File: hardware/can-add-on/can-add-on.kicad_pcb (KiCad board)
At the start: 2 copper layers, 48 x 40 mm, 32 parts

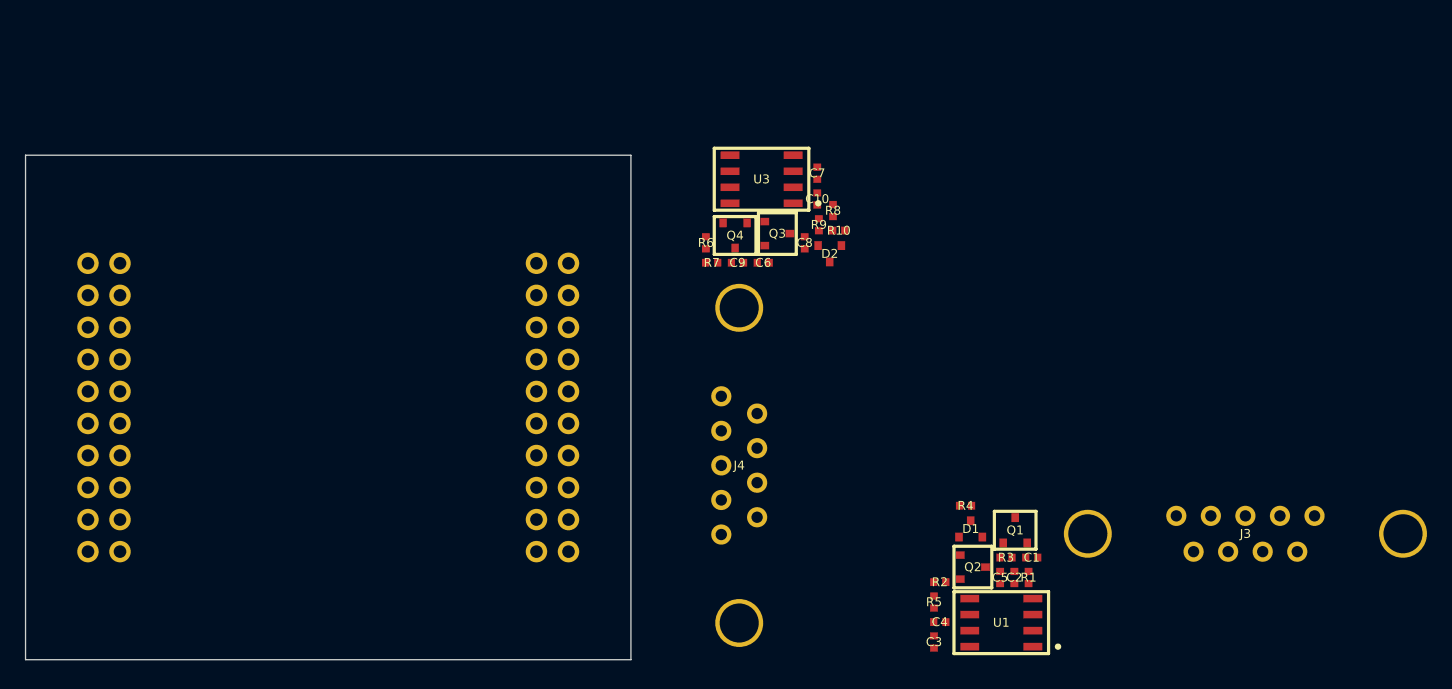
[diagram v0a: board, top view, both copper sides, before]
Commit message: Factor out glasgow
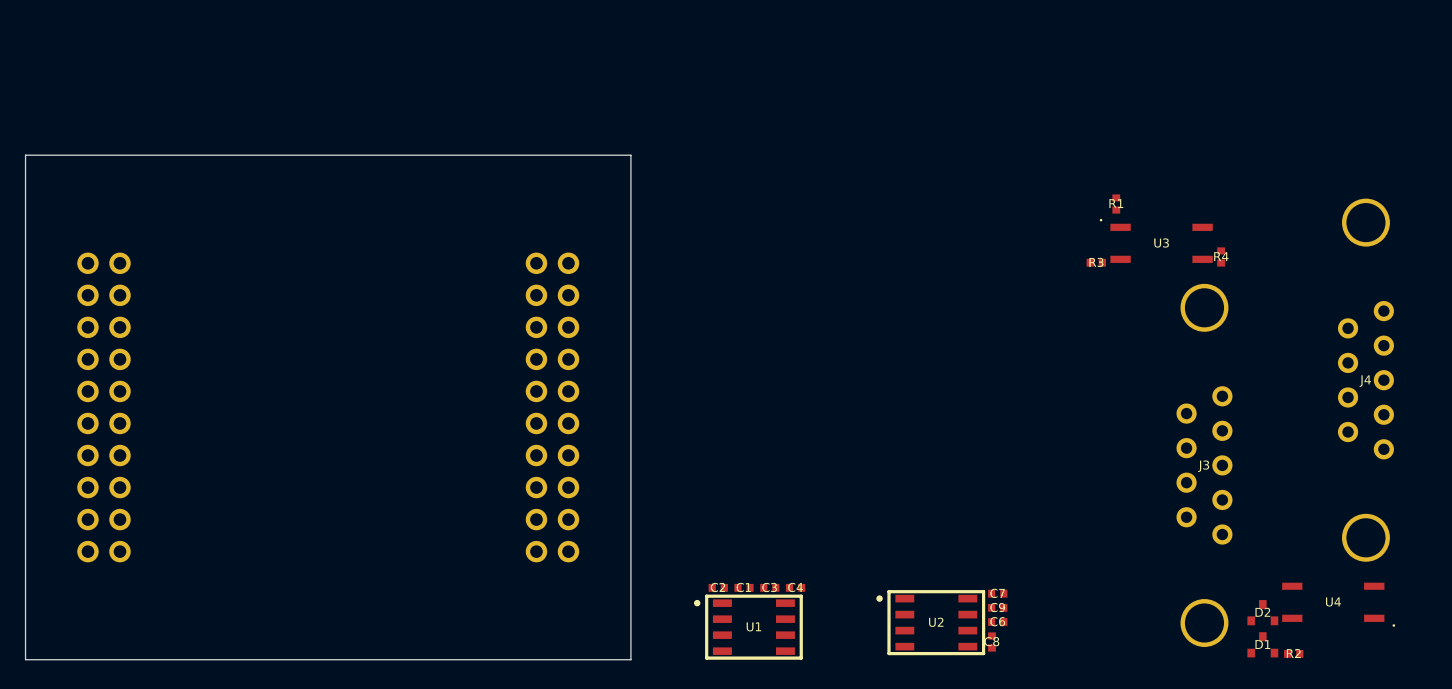
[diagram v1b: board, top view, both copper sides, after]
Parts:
- removed C10, C5, R10, R5, R6, R7, R8, R9: , can-add-on:ipc-two-pin-package$22
- removed Q1, Q2, Q3, Q4: , can-add-on:SOT95P280X100-3N
- added U2: , can-add-on:soic127p-package$19, F.Cu at (196.7, 122.1)
- added U4: , can-add-on:tlp-175, F.Cu at (228.2, 120.4)
- C1, C2, C3, C4, C6, C7, C8, C9, R1, R2, R3, R4: footprint can-add-on:ipc-two-pin-package$22 -> can-add-on:ipc-two-pin-package$24
- J1, J2: footprint can-add-on:pin-header-pkg$13 -> can-add-on:pin-header-pkg$15
- J3, J4: footprint can-add-on:amphenol-delta-d-pkg$30 -> can-add-on:amphenol-delta-d-pkg$32
- U1: footprint can-add-on:soic127p-package$17 -> can-add-on:soic127p-package$19
- U3: footprint can-add-on:soic127p-package$17 -> can-add-on:tlp-175
- moved J4 50.2 mm to (230.8, 102.8), turned to 0 degrees
- moved D2 44.6 mm to (222.6, 121.3), turned to 0 degrees
- moved C7 36.3 mm to (201.6, 119.8), turned to 0 degrees
- moved C8 35.0 mm to (201.1, 123.6), turned to 90 degrees
- moved C9 34.3 mm to (201.6, 120.9), turned to 180 degrees
- moved C6 34.0 mm to (201.6, 122.0)
- moved U3 32.1 mm to (214.6, 92.0), turned to 0 degrees
- moved R1 30.4 mm to (211.0, 88.9)
- moved R2 28.6 mm to (225.1, 124.5), turned to 0 degrees
- moved R4 28.3 mm to (219.3, 93.1), turned to 90 degrees
- moved D1 24.9 mm to (222.6, 123.8)
- moved R3 24.4 mm to (209.4, 93.5)
- moved C2 23.5 mm to (179.4, 119.3), turned to 0 degrees
- moved C1 22.9 mm to (181.5, 119.3), turned to 180 degrees
- moved U1 19.6 mm to (182.3, 122.4), turned to 0 degrees
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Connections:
- net net_can-a_vcc renamed net_xr-a_vcc
- C6 pad 1: net_can-b_vcc -> net_xr-b_vio
- C7 pad 1: net_can-b_vcc -> net_xr-b_vio
- C8 pad 1: net_can-b_vcc -> net_xr-b_vio
- C9 pad 1: net_can-b_vcc -> net_xr-b_vio
- D1 pad 1: net_can-a_j_p3 -> net_xr-a_can_canh
- D1 pad 2: net_can-a_xr_xcvr_CANL -> net_ssr$38_drain1
- D2 pad 1: net_can-b_xr_xcvr_CANH -> net_j-b_p3
- D2 pad 2: net_can-b_rid$39_p1 -> net_j-b_p5
- J1 pad 1: net_can-b_vcc -> net_xr-b_vio
- J3 pad 3: net_can-a_j_p3 -> net_xr-a_can_canh
- J3 pad 5: net_can-a_xr_xcvr_CANL -> net_ssr$38_drain1
- J4 pad 3: net_can-b_xr_xcvr_CANH -> net_j-b_p3
- J4 pad 5: net_can-b_rid$39_p1 -> net_j-b_p5
- R1 pad 1: net_can-a_j_p3 -> glasgow_PA4
- R1 pad 2: net_can-a_rid$36_p2 -> net_ssr$38_a
- R2 pad 1: net_can-a_xr_xcvr_CANL -> net_j-b_p3
- R2 pad 2: net_can-a_q$33_1_s -> net_ssr$46_drain2
- R3 pad 1: glasgow_PA3 -> net_xr-a_can_canh
- R3 pad 2: net_can-a_rid$42_p1 -> net_ssr$38_drain2
- R4 pad 1: net_can-a_rid$42_p1 -> glasgow_PB4
- R4 pad 2: gnd -> net_ssr$46_a
- U1 pad 6: net_can-a_xr_xcvr_CANL -> net_ssr$38_drain1
- U1 pad 7: net_can-a_j_p3 -> net_xr-a_can_canh
- U1 pad 8: glasgow_PA4 -> glasgow_PA3
- U3 pad 1: glasgow_PB1 -> net_ssr$38_a
- U3 pad 3: net_can-b_vcc -> gnd
- U3 pad 4: glasgow_PB2 -> net_ssr$38_drain2
- U3 pad 6: net_can-b_rid$39_p1 -> net_ssr$38_drain1

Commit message: REfactor glasgow model
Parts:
- removed D2: , can-add-on:SC-70-3
- added ?: , can-add-on:two-pin-polarized-package$58, F.Cu at (202.7, 79.7)
- added ?: , can-add-on:two-pin-polarized-package$58, F.Cu at (201.8, 81.7)
- added C10: , can-add-on:ipc-two-pin-package$30, F.Cu at (205.7, 81.7)
- added C11: , can-add-on:ipc-two-pin-package$30, F.Cu at (192.5, 123.6)
- added C12: , can-add-on:ipc-two-pin-package$30, F.Cu at (199.5, 80.1)
- added C5: , can-add-on:ipc-two-pin-package$30, F.Cu at (193.7, 100.9)
- added D4: , can-add-on:SC-70-3, F.Cu at (194.5, 103.2)
- added T1: , can-add-on:xfmr-760390012, F.Cu at (214.3, 115.9)
- added U5: , can-add-on:soic127p-package$65, F.Cu at (197.1, 118.7)
- added U6: , can-add-on:tlp-175, F.Cu at (194.1, 110.7)
- C1, C2, C3, C4, C6, C7, C8, C9, R1, R2, R3, R4: footprint can-add-on:ipc-two-pin-package$24 -> can-add-on:ipc-two-pin-package$30
- J1, J2: footprint can-add-on:pin-header-pkg$15 -> can-add-on:pin-header-pkg$19
- J3, J4: footprint can-add-on:amphenol-delta-d-pkg$32 -> can-add-on:amphenol-delta-d-pkg$38
- U1: footprint can-add-on:soic127p-package$19 -> can-add-on:soic127p-package$25
- U2: footprint can-add-on:soic127p-package$19 -> can-add-on:tlp-175
- U3: footprint can-add-on:tlp-175 -> can-add-on:soic127p-package$25
- U4: footprint can-add-on:tlp-175 -> can-add-on:SOT95P280X145-5N
- moved D1 49.5 mm to (197.2, 81.3), turned to 90 degrees
- moved R2 46.0 mm to (207.3, 82.2)
- moved U2 45.0 mm to (210.4, 79.2)
- moved C9 42.3 mm to (196.5, 78.9), turned to 270 degrees
- moved C8 41.9 mm to (199.1, 81.7)
- moved U3 31.3 mm to (206.0, 122.1)
- moved R4 28.5 mm to (193.7, 105.5)
- moved J4 25.4 mm to (205.8, 98.2)
- moved R3 24.1 mm to (197.2, 114.3)
- moved U4 24.1 mm to (204.3, 118.1), turned to 90 degrees
- moved C6 18.8 mm to (192.5, 105.5), turned to 270 degrees
- moved C7 15.8 mm to (194.8, 105.5), turned to 90 degrees
- moved J3 14.0 mm to (212.2, 96.8), turned to 180 degrees
- moved R1 9.61 mm to (204.6, 81.7)
- moved C1 6.65 mm to (185.6, 124.5), turned to 0 degrees
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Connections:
- net glasgow_PA1 renamed CANA-TX
- net glasgow_PA2 renamed CANA-RX
- net glasgow_PA3 renamed CANA-S
- net net_xr-a_vcc renamed VIO-A
- C6 pad 1: net_xr-b_vio -> VIO-B
- C7 pad 1: net_xr-b_vio -> VIO-B
- C8 pad 1: net_xr-b_vio -> VIO-B
- C9 pad 1: net_xr-b_vio -> net_iso$61_en2
- C9 pad 2: gnd -> net_iso$61_iso_GND2
- D1 pad 1: net_xr-a_can_canh -> CANA-H
- D1 pad 2: net_ssr$38_drain1 -> CANA-L
- J1 pad 1: net_xr-b_vio -> VIO-B
- J3 pad 3: net_xr-a_can_canh -> CANA-H
- J3 pad 5: net_ssr$38_drain1 -> CANA-L
- J4 pad 3: net_j-b_p3 -> net_rid$71_p1
- R1 pad 2: net_ssr$38_a -> net_ssr$44_a
- R2 pad 1: net_j-b_p3 -> CANA-H
- R2 pad 2: net_ssr$46_drain2 -> net_rid$49_p2
- R3 pad 1: net_xr-a_can_canh -> glasgow_PB4
- R3 pad 2: net_ssr$38_drain2 -> net_ssr$69_a
- R4 pad 1: glasgow_PB4 -> net_rid$71_p1
- R4 pad 2: net_ssr$46_a -> net_rid$71_p2
- U1 pad 6: net_ssr$38_drain1 -> CANA-L
- U1 pad 7: net_xr-a_can_canh -> CANA-H
- U2 pad 1: glasgow_PB1 -> net_ssr$44_a
- U2 pad 3: net_xr-b_vio -> gnd
- U2 pad 4: glasgow_PB2 -> net_rid$49_p2
- U2 pad 6: net_j-b_p5 -> CANA-L
- U3 pad 1: net_ssr$38_a -> net_xr-b_uart_tx
- U3 pad 3: gnd -> VIO-B
- U3 pad 4: net_ssr$38_drain2 -> net_xr-b_uart_rx
- U3 pad 6: net_ssr$38_drain1 -> net_j-b_p5
- U4 pad 1: net_ssr$46_a -> net_iso$51_xfrmr_p5
- U4 pad 3: gnd -> net_iso$51_xfrmr_p1
- U4 pad 4: net_ssr$46_drain2 -> gnd

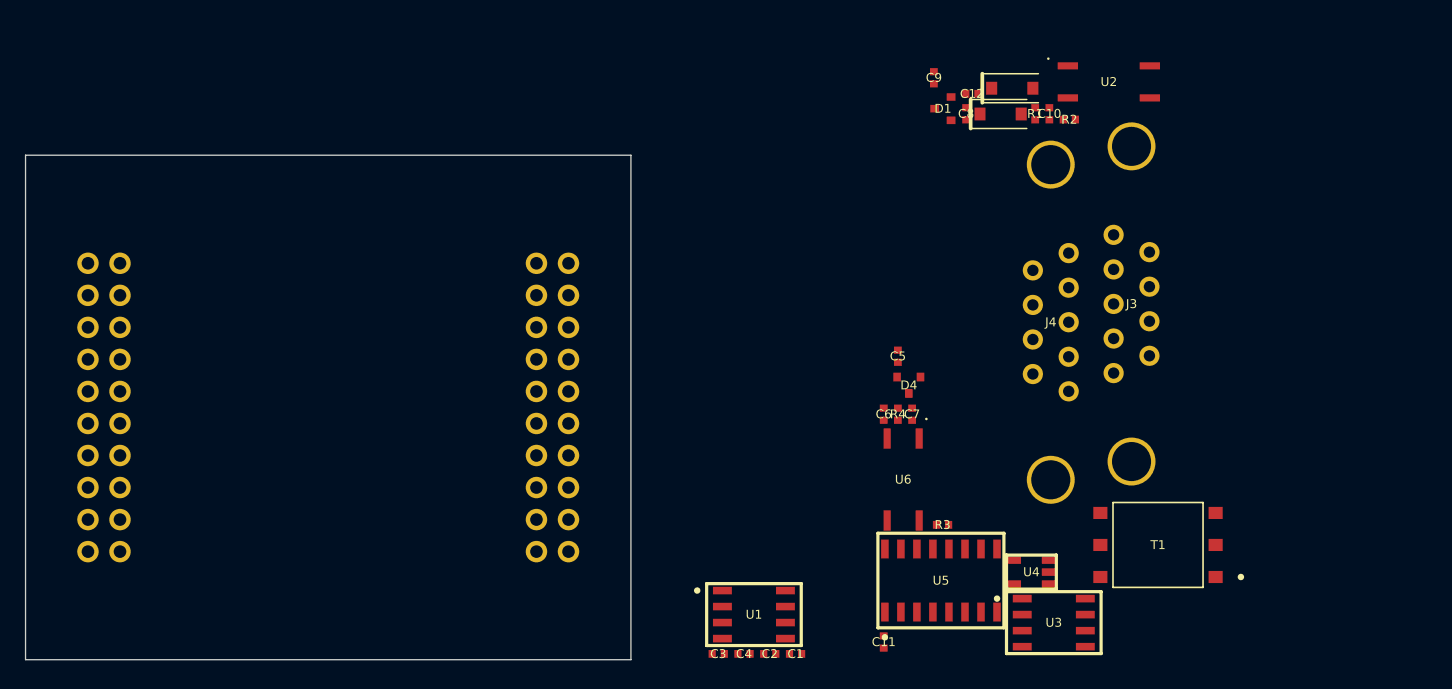
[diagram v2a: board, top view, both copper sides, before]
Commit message: Update gnd connections for isolation
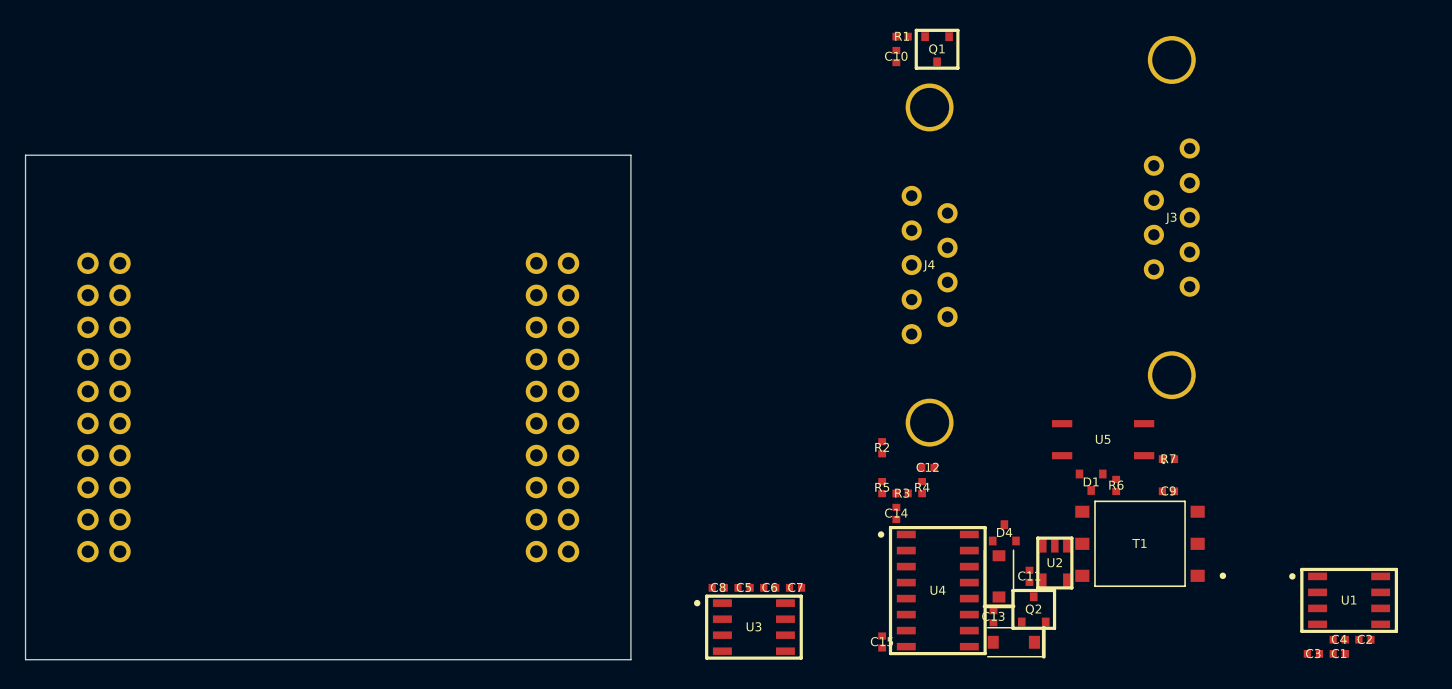
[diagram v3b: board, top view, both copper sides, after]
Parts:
- removed the ? at (202.7, 79.7)
- removed the ? at (201.8, 81.7)
- removed U6: , can-add-on:tlp-175
- added ?: , can-add-on:two-pin-polarized-package$68, F.Cu at (201.7, 118.4)
- added ?: , can-add-on:two-pin-polarized-package$68, F.Cu at (202.9, 123.6)
- added C13: , can-add-on:ipc-two-pin-package$30, F.Cu at (201.2, 121.6)
- added C14: , can-add-on:ipc-two-pin-package$30, F.Cu at (193.5, 113.4)
- added C15: , can-add-on:ipc-two-pin-package$30, F.Cu at (192.4, 123.6)
- added Q1: , can-add-on:SOT95P280X100-3N, F.Cu at (196.8, 76.6)
- added Q2: , can-add-on:SOT95P280X100-3N, F.Cu at (204.4, 121.0)
- added R5: , can-add-on:ipc-two-pin-package$30, F.Cu at (192.4, 111.4)
- added R6: , can-add-on:ipc-two-pin-package$30, F.Cu at (211.0, 111.2)
- added R7: , can-add-on:ipc-two-pin-package$30, F.Cu at (215.1, 109.1)
- U2: footprint can-add-on:tlp-175 -> can-add-on:SOT95P280X145-5N
- U4: footprint can-add-on:SOT95P280X145-5N -> can-add-on:soic127p-package$75
- U5: footprint can-add-on:soic127p-package$65 -> can-add-on:tlp-175
- moved U1 47.2 mm to (229.4, 120.3)
- moved C2 47.2 mm to (230.7, 123.4)
- moved C4 47.2 mm to (228.7, 123.4)
- moved C3 47.2 mm to (226.6, 124.5)
- moved C1 43.1 mm to (228.7, 124.5)
- moved C8 42.4 mm to (179.4, 119.3), turned to 0 degrees
- moved U2 38.4 mm to (206.1, 117.3), turned to 180 degrees
- moved C9 37.7 mm to (215.1, 111.6), turned to 0 degrees
- moved D1 31.9 mm to (209.0, 110.9), turned to 180 degrees
- moved R2 30.0 mm to (192.4, 108.2), turned to 270 degrees
- moved C12 29.9 mm to (196.0, 109.8), turned to 180 degrees
- moved U3 23.8 mm to (182.3, 122.4)
- moved C5 22.0 mm to (181.5, 119.3), turned to 0 degrees
- moved U5 17.0 mm to (209.9, 107.6), turned to 180 degrees
- moved C7 16.6 mm to (185.6, 119.3), turned to 0 degrees
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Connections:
- C10 pad 1: VIO-B -> CANA-H
- C11 pad 1: VIO-B -> VIO-B-ISO
- C11 pad 2: gnd -> net_xr-b_gnd
- C12 pad 1: net_iso$61_en2 -> net_q$44_0_d
- C12 pad 2: net_iso$61_iso_GND2 -> gnd
- C5 pad 1: VIO-B -> VIO-B-ISO
- C5 pad 2: gnd -> net_xr-b_gnd
- C6 pad 1: VIO-B -> VIO-B-ISO
- C6 pad 2: gnd -> net_xr-b_gnd
- C7 pad 1: VIO-B -> VIO-B-ISO
- C7 pad 2: gnd -> net_xr-b_gnd
- C8 pad 1: VIO-B -> VIO-B-ISO
- C8 pad 2: gnd -> net_xr-b_gnd
- C9 pad 1: net_iso$61_en2 -> CANA-L
- C9 pad 2: net_iso$61_iso_GND2 -> gnd
- D4 pad 1: net_rid$71_p1 -> net_j-b_p3
- D4 pad 2: net_j-b_p5 -> net_ssr$79_drain1
- D4 pad 3: gnd -> net_xr-b_gnd
- J1 pad 1: VIO-B -> net_iso$71_en1
- J4 pad 10: gnd -> net_xr-b_gnd
- J4 pad 11: gnd -> net_xr-b_gnd
- J4 pad 2: gnd -> net_xr-b_gnd
- J4 pad 3: net_rid$71_p1 -> net_j-b_p3
- J4 pad 5: net_j-b_p5 -> net_ssr$79_drain1
- R1 pad 1: glasgow_PA4 -> CANA-H
- R1 pad 2: net_ssr$44_a -> net_q$44_0_s
- R2 pad 1: CANA-H -> CANA-L
- R3 pad 1: glasgow_PB4 -> glasgow_PA4
- R3 pad 2: net_ssr$69_a -> net_q$44_0_g
- R4 pad 1: net_rid$71_p1 -> net_q$44_0_g
- R4 pad 2: net_rid$71_p2 -> gnd
- T1 pad 1: net_iso$51_xfrmr_p1 -> net_iso$61_xfrmr_p1
- T1 pad 2: VIO-B -> net_iso$71_en1
- T1 pad 3: net_iso$51_xfrmr_p3 -> net_iso$61_xfrmr_p3
- T1 pad 4: net_iso$61_iso_GND2 -> net_xr-b_gnd
- T1 pad 5: net_iso$51_xfrmr_p5 -> net_iso$61_xfrmr_p5
- T1 pad 6: net_iso$51_xfrmr_p6 -> net_iso$61_xfrmr_p6
- U2 pad 1: net_ssr$44_a -> net_iso$61_xfrmr_p5
- U2 pad 3: gnd -> net_iso$61_xfrmr_p1
- U2 pad 4: net_rid$49_p2 -> gnd
- U3 pad 2: gnd -> net_xr-b_gnd
- U3 pad 3: VIO-B -> VIO-B-ISO
- U3 pad 5: VIO-B -> VIO-B-ISO
- U3 pad 6: net_j-b_p5 -> net_ssr$79_drain1
- U3 pad 7: net_rid$71_p1 -> net_j-b_p3
- U4 pad 1: net_iso$51_xfrmr_p5 -> net_iso$71_en1
- U4 pad 2: VIO-B -> gnd
- U4 pad 3: net_iso$51_xfrmr_p1 -> glasgow_PB1
- U4 pad 4: gnd -> glasgow_PB3
- U4 pad 5: gnd -> net_iso$71_vdd1-in2
- U5 pad 1: VIO-B -> net_ssr$79_a
- U5 pad 3: glasgow_PB1 -> gnd
- U5 pad 4: glasgow_PB3 -> net_ssr$79_drain2
- U5 pad 6: glasgow_PB2 -> net_ssr$79_drain1

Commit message: Update ocdb to fix fet symbols
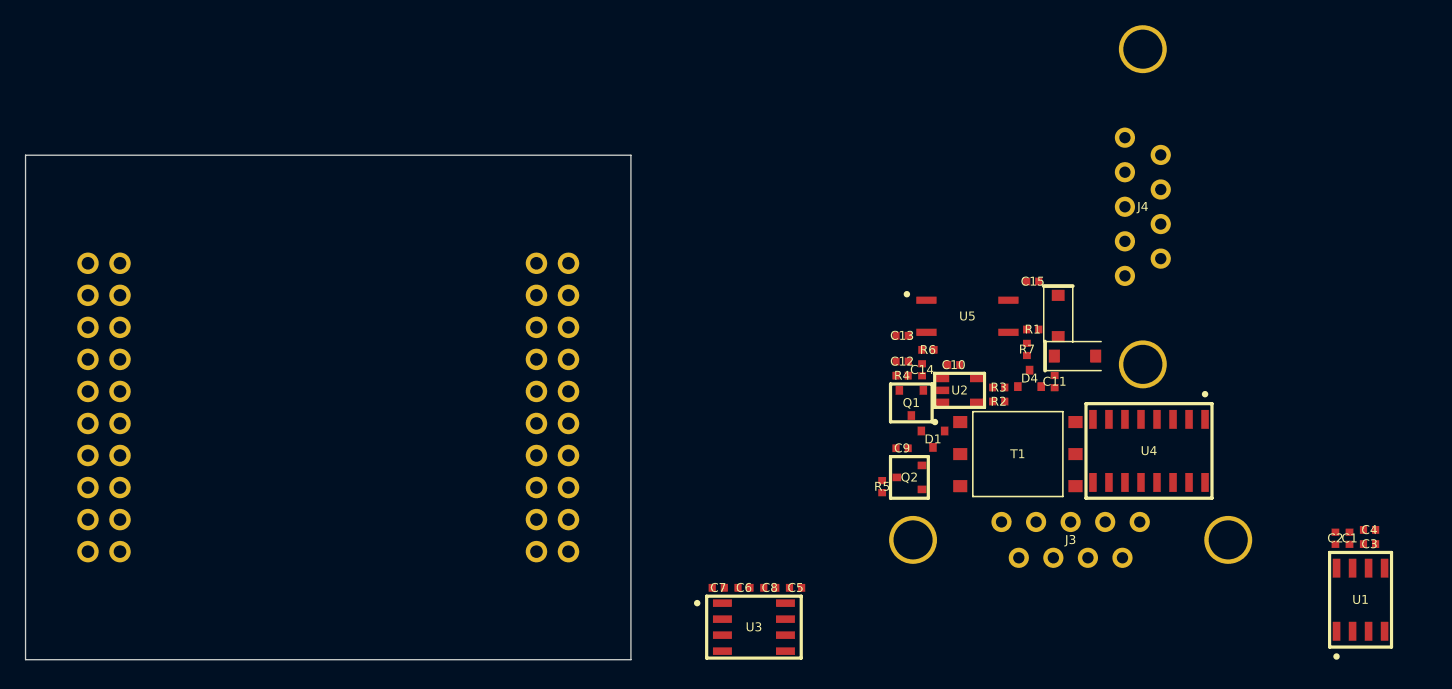
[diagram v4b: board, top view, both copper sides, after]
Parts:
- removed the ? at (201.7, 118.4)
- removed the ? at (202.9, 123.6)
- added ?: , can-add-on:two-pin-polarized-package$68, F.Cu at (206.4, 97.7)
- added ?: , can-add-on:two-pin-polarized-package$68, F.Cu at (207.7, 100.9)
- moved C15 31.0 mm to (204.4, 95.0), turned to 180 degrees
- moved Q1 28.1 mm to (194.7, 104.6)
- moved J3 26.8 mm to (207.4, 115.5), turned to 90 degrees
- moved R1 25.4 mm to (204.4, 98.8)
- moved C10 24.9 mm to (198.1, 101.6), turned to 0 degrees
- moved C13 23.4 mm to (194.0, 99.3), turned to 180 degrees
- moved C9 21.4 mm to (194.0, 108.2)
- moved U4 20.1 mm to (213.6, 108.4), turned to 270 degrees
- moved R6 18.4 mm to (196.0, 100.4), turned to 180 degrees
- moved J4 17.5 mm to (213.1, 89.1)
- moved U2 15.6 mm to (198.6, 103.6), turned to 270 degrees
- moved C11 15.6 mm to (206.1, 103.0)
- moved U5 14.5 mm to (199.2, 97.8), turned to 0 degrees
- moved Q2 14.4 mm to (194.6, 110.5), turned to 90 degrees
- moved R7 14.2 mm to (203.9, 100.4), turned to 90 degrees
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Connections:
- T1 pad 4: net_xr-b_gnd -> net_iso$61_xfrmr_p4
- T1 pad 5: net_iso$61_xfrmr_p5 -> net_xr-b_gnd
- U2 pad 1: net_iso$61_xfrmr_p5 -> net_iso$61_xfrmr_p3
